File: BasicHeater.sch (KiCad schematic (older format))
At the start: 10 parts, among them J13 Thermistor

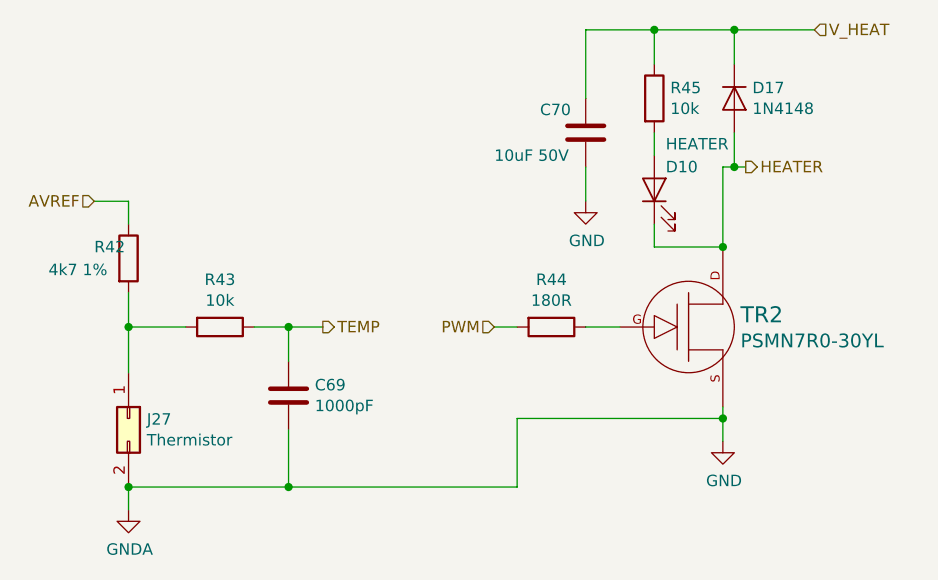
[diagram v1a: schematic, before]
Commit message: Change LED value to LED from HEATER.
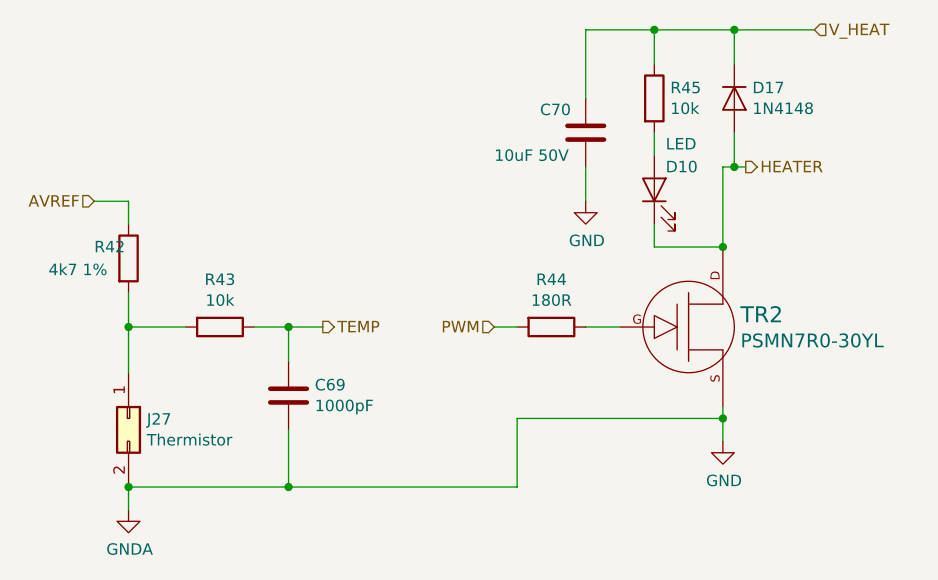
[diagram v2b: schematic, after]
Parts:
- D2: value HEATER -> LED
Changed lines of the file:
@@
 AR Path="/5AB8F10D/5ACEEAB5" Ref="D11"  Part="1"
 F 0 "D10" V 5350 2600 50  0000 R CNN
-F 1 "HEATER" V 5450 2600 50  0000 R CNN
+F 1 "LED" V 5450 2600 50  0000 R CNN
 F 2 "PrntrBoardV1:LED_0603_1608Metric" H 5250 2650 50  0001 C CNN
 F 3 "~" H 5250 2650 50  0001 C CNN

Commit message: Switch away from rounded rect pads. The PCB boar house had issues making the board.
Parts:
- C16: footprint Capacitor_SMD:C_0603_1608Metric -> PrntrBoardV1:C_0603_1608Metric
- C17: footprint Capacitor_SMD:C_1206_3216Metric -> PrntrBoardV1:C_1206_3216Metric
- R10, R11, R8, R9: footprint Resistor_SMD:R_0603_1608Metric -> PrntrBoardV1:R_0603_1608Metric
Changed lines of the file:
@@
 F 0 "R42" H 2800 3000 50  0000 L CNN
 F 1 "4k7 1%" H 2600 2900 50  0000 L CNN
-F 2 "Resistor_SMD:R_0603_1608Metric" V 2880 2950 50  0001 C CNN
+F 2 "PrntrBoardV1:R_0603_1608Metric" V 2880 2950 50  0001 C CNN
 F 3 "~" H 2950 2950 50  0001 C CNN
 	1    2950 2950
@@
 F 0 "R43" V 3143 3250 50  0000 C CNN
 F 1 "10k" V 3234 3250 50  0000 C CNN
-F 2 "Resistor_SMD:R_0603_1608Metric" V 3280 3250 50  0001 C CNN
+F 2 "PrntrBoardV1:R_0603_1608Metric" V 3280 3250 50  0001 C CNN
 F 3 "~" H 3350 3250 50  0001 C CNN
 	1    3350 3250
@@
 F 0 "C69" H 3765 3596 50  0000 L CNN
 F 1 "1000pF" H 3765 3505 50  0000 L CNN
-F 2 "Capacitor_SMD:C_0603_1608Metric" H 3688 3400 50  0001 C CNN
+F 2 "PrntrBoardV1:C_0603_1608Metric" H 3688 3400 50  0001 C CNN
 F 3 "~" H 3650 3550 50  0001 C CNN
 	1    3650 3550
@@
 F 0 "R44" V 4593 3250 50  0000 C CNN
 F 1 "180R" V 4684 3250 50  0000 C CNN
-F 2 "Resistor_SMD:R_0603_1608Metric" V 4730 3250 50  0001 C CNN
+F 2 "PrntrBoardV1:R_0603_1608Metric" V 4730 3250 50  0001 C CNN
 F 3 "~" H 4800 3250 50  0001 C CNN
 	1    4800 3250
@@
 F 0 "C70" H 4750 2500 50  0000 L CNN
 F 1 "10uF 50V" H 4550 2300 50  0000 L CNN
-F 2 "Capacitor_SMD:C_1206_3216Metric" H 4950 2400 50  0001 C CNN
+F 2 "PrntrBoardV1:C_1206_3216Metric" H 4950 2400 50  0001 C CNN
 F 3 "~" H 4950 2400 50  0001 C CNN
 	1    4950 2400
@@
 F 0 "R45" H 5320 2296 50  0000 L CNN
 F 1 "10k" H 5320 2205 50  0000 L CNN
-F 2 "Resistor_SMD:R_0603_1608Metric" V 5180 2250 50  0001 C CNN
+F 2 "PrntrBoardV1:R_0603_1608Metric" V 5180 2250 50  0001 C CNN
 F 3 "~" H 5250 2250 50  0001 C CNN
 	1    5250 2250

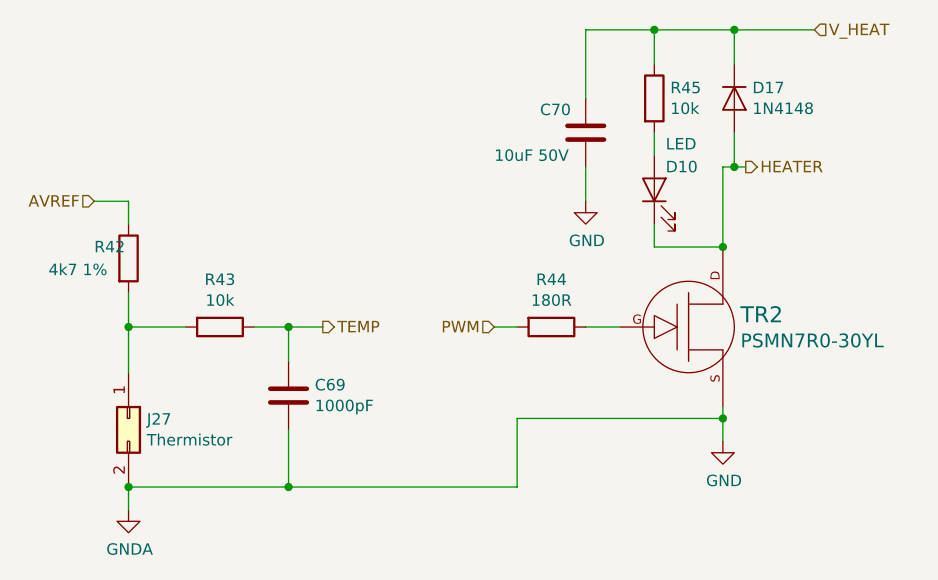
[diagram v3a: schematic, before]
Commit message: Update thermistor filter capacitor values.
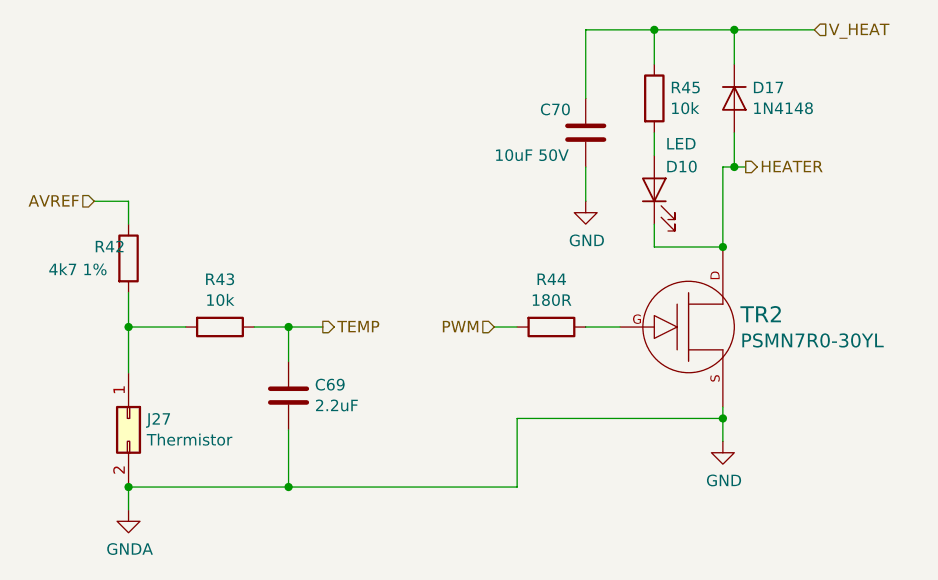
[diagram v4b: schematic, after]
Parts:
- C16: value 1000pF -> 2.2uF
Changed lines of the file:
@@
 AR Path="/5AB8F10D/5AD4D569" Ref="C71"  Part="1"
 F 0 "C69" H 3765 3596 50  0000 L CNN
-F 1 "1000pF" H 3765 3505 50  0000 L CNN
+F 1 "2.2uF" H 3765 3505 50  0000 L CNN
 F 2 "PrntrBoardV1:C_0603_1608Metric" H 3688 3400 50  0001 C CNN
 F 3 "~" H 3650 3550 50  0001 C CNN
